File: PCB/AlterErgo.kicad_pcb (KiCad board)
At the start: 2 copper layers, 104 parts, among them J1 GS3, J2 SJ-43514, J3 GS3, J4 Conn_01x02, SW0:10 SW_Push, SW0:11 SW_Push, SW0:12 SW_Push, SW0:7 SW_Push, SW0:8 SW_Push, SW0:9 SW_Push, SW1 SW_SPST, SW1:10 SW_Push, SW1:11 SW_Push, SW1:12 SW_Push, SW1:13 SW_Push, SW1:7 SW_Push, SW1:8 SW_Push, SW1:9 SW_Push, SW2:10 SW_Push, SW2:11 SW_Push, SW2:12 SW_Push, SW2:13 SW_Push, SW2:7 SW_Push, SW2:8 SW_Push, SW2:9 SW_Push, SW3:10 SW_Push, SW3:11 SW_Push, SW3:12 SW_Push, SW3:13 SW_Push, SW3:8 SW_Push, SW3:9 SW_Push, SW4:10 SW_Push, SW4:11 SW_Push, SW4:12 SW_Push, SW4:13 SW_Push, SW4:7 SW_Push, SW4:8 SW_Push, SW4:9 SW_Push, SW5:10 SW_Push, SW5:11 SW_Push, SW5:12 SW_Push, SW5:13 SW_Push, SW5:7 SW_Push, SW5:8 SW_Push, SW5:9 SW_Push, U1 Feather32u4Bluefruit, U2 MCP23018

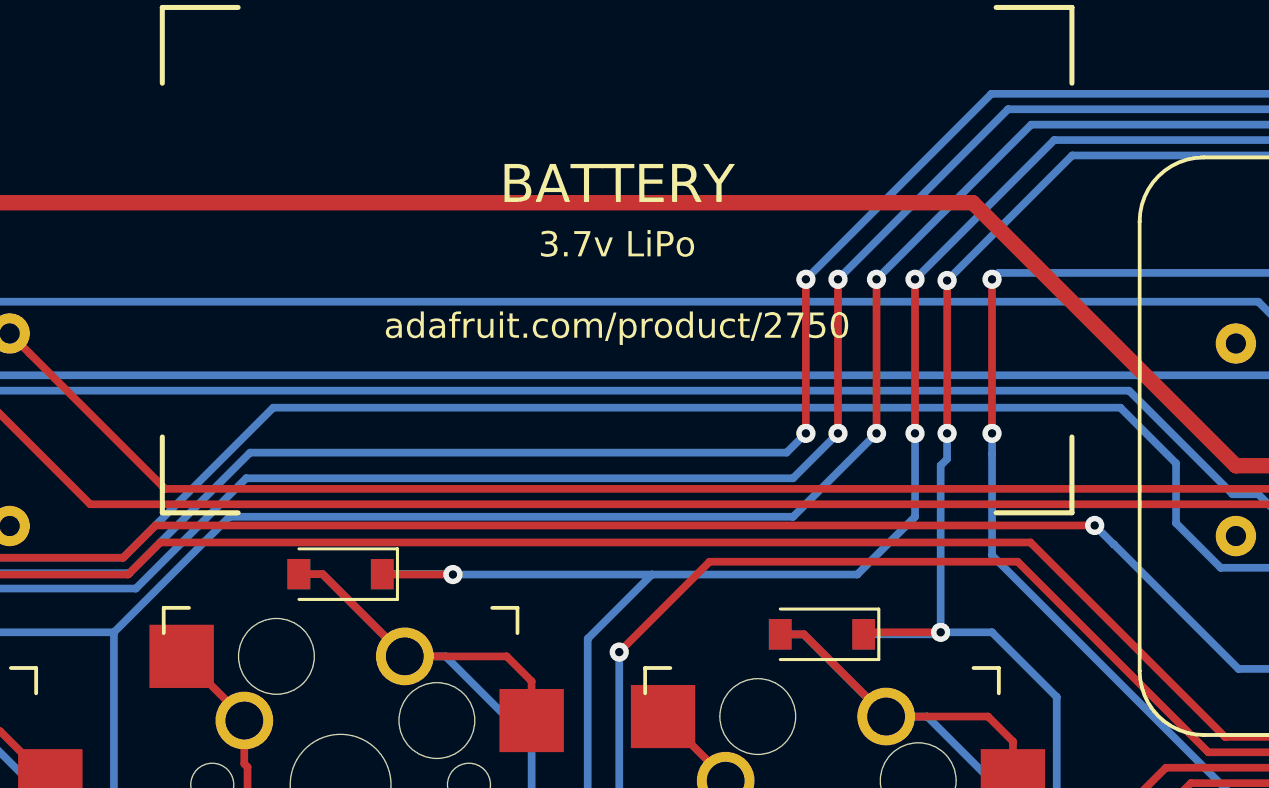
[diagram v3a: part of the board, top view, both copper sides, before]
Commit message: Correct some vias too close to other tracks
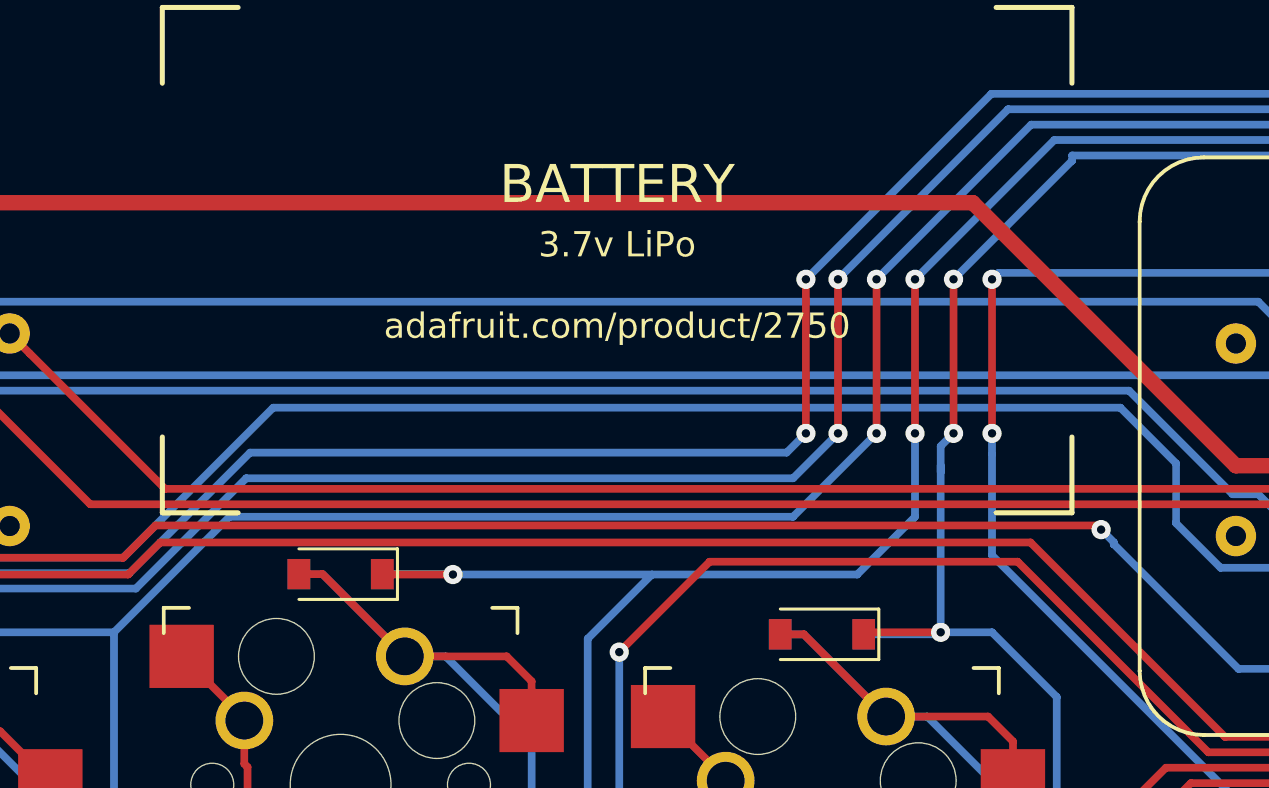
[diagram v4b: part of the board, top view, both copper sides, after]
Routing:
- net (no net): track 98.3 -> 29.2 mm
- net Net-(D1:13-Pad2): track 37.9 -> 59.3 mm
- net Net-(D4:13-Pad2): track 42.2 -> 60.0 mm
- net Net-(D3:13-Pad2): track 42.9 -> 60.4 mm
- net Net-(D2:13-Pad2): track 46.5 -> 58.8 mm
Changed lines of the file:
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@@
   (general
     (links 466)
-    (no_connects 453)
+    (no_connects 20)
     (area 33.589001 -2.08962 221.067701 182.523514)
     (thickness 1.6)
     (drawings 68)
-    (tracks 1728)
+    (tracks 1733)
     (zones 0)
     (modules 104)
@@
   (segment (start 192.7225 125.25375) (end 192.7225 118.070951) (width 0.3048) (layer F.Cu) (net 0))
   (segment (start 202.565 144.30375) (end 202.565 136.68375) (width 0.3048) (layer F.Cu) (net 0))
-  (segment (start 194.8815 133.477) (end 193.3575 131.953) (width 0.3048) (layer B.Cu) (net 0))
-  (segment (start 204.2795 133.477) (end 194.8815 133.477) (width 0.3048) (layer B.Cu) (net 0))
-  (segment (start 205.105 134.3025) (end 204.2795 133.477) (width 0.3048) (layer B.Cu) (net 0))
-  (segment (start 205.105 137.95375) (end 205.105 134.3025) (width 0.3048) (layer B.Cu) (net 0))
-  (segment (start 205.105 143.03375) (end 205.105 137.95375) (width 0.3048) (layer B.Cu) (net 0))
-  (segment (start 193.1035 113.157) (end 198.4375 113.157) (width 0.3048) (layer F.Cu) (net 0))
-  (segment (start 190.1825 116.078) (end 193.1035 113.157) (width 0.3048) (layer F.Cu) (net 0))
-  (segment (start 190.1825 118.90375) (end 190.1825 116.078) (width 0.3048) (layer F.Cu) (net 0))
-  (segment (start 192.3415 94.107) (end 198.1835 94.107) (width 0.3048) (layer B.Cu) (net 0))
-  (segment (start 190.1825 96.266) (end 192.3415 94.107) (width 0.3048) (layer B.Cu) (net 0))
-  (segment (start 190.1825 104.93375) (end 190.1825 96.266) (width 0.3048) (layer B.Cu) (net 0))
-  (segment (start 192.3415 75.057) (end 198.4375 75.057) (width 0.3048) (layer B.Cu) (net 0))
-  (segment (start 190.1825 77.216) (end 192.3415 75.057) (width 0.3048) (layer B.Cu) (net 0))
-  (segment (start 190.1825 85.88375) (end 190.1825 77.216) (width 0.3048) (layer B.Cu) (net 0))
   (segment (start 54.1655 128.905) (end 57.9755 128.905) (width 0.3048) (layer F.Cu) (net 1))
   (segment (start 57.9755 128.905) (end 68.1355 118.745) (width 0.3048) (layer F.Cu) (net 1))
@@
   (segment (start 108.7125 139.064808) (end 106.165876 139.064808) (width 0.3048) (layer F.Cu) (net 8))
   (segment (start 106.165876 139.064808) (end 105.523159 139.707525) (width 0.3048) (layer F.Cu) (net 8))
+  (segment (start 161.8615 39.751) (end 161.8615 40.005) (width 0.3048) (layer B.Cu) (net 9))
+  (segment (start 161.8615 40.005) (end 161.8615 46.355) (width 0.3048) (layer B.Cu) (net 9))
+  (segment (start 162.3695 38.481) (end 161.8615 38.989) (width 0.3048) (layer B.Cu) (net 9))
+  (segment (start 161.8615 38.989) (end 161.8615 40.005) (width 0.3048) (layer B.Cu) (net 9))
+  (segment (start 162.3695 38.227) (end 162.3695 38.481) (width 0.3048) (layer F.Cu) (net 9))
+  (via (at 162.3695 38.481) (size 0.762) (drill 0.3302) (layers F.Cu B.Cu) (net 9))
+  (segment (start 162.3695 32.385) (end 162.3695 38.227) (width 0.3048) (layer F.Cu) (net 9))
+  (segment (start 167.065425 27.482799) (end 167.065425 27.689075) (width 0.3048) (layer B.Cu) (net 9))
+  (segment (start 167.065425 27.689075) (end 162.3695 32.385) (width 0.3048) (layer B.Cu) (net 9))
+  (via (at 162.3695 32.385) (size 0.762) (drill 0.3302) (layers F.Cu B.Cu) (net 9))
   (segment (start 166.454701 48.916201) (end 166.454701 60.557799) (width 0.3048) (layer B.Cu) (net 9))
   (segment (start 93.69375 151.447692) (end 93.69375 152.43125) (width 0.3048) (layer B.Cu) (net 9))
@@
   (segment (start 161.988499 65.024001) (end 161.6075 65.405) (width 0.3048) (layer B.Cu) (net 9))
   (segment (start 161.8615 46.355) (end 163.8935 46.355) (width 0.3048) (layer B.Cu) (net 9))
-  (segment (start 162.1155 39.497) (end 161.8615 39.751) (width 0.3048) (layer B.Cu) (net 9))
-  (segment (start 161.8615 39.751) (end 161.8615 46.355) (width 0.3048) (layer B.Cu) (net 9))
   (segment (start 161.6075 122.555) (end 158.891875 122.555) (width 0.3048) (layer F.Cu) (net 9))
   (segment (start 158.891875 122.555) (end 158.8125 122.634375) (width 0.3048) (layer F.Cu) (net 9))
@@
   (segment (start 161.782125 46.434375) (end 161.8615 46.355) (width 0.3048) (layer B.Cu) (net 9))
   (via (at 161.8615 46.355) (size 0.762) (drill 0.3302) (layers F.Cu B.Cu) (net 9))
-  (segment (start 162.1155 38.481) (end 162.1155 39.497) (width 0.3048) (layer B.Cu) (net 9))
-  (segment (start 162.1155 32.432724) (end 162.1155 38.481) (width 0.3048) (layer F.Cu) (net 9))
-  (via (at 162.1155 38.481) (size 0.762) (drill 0.3302) (layers F.Cu B.Cu) (net 9))
   (segment (start 193.8655 28.829) (end 192.519299 27.482799) (width 0.3048) (layer B.Cu) (net 9))
   (segment (start 192.519299 27.482799) (end 167.065425 27.482799) (width 0.3048) (layer B.Cu) (net 9))
-  (segment (start 167.065425 27.482799) (end 162.1155 32.432724) (width 0.3048) (layer B.Cu) (net 9))
-  (via (at 162.1155 32.432724) (size 0.762) (drill 0.3302) (layers F.Cu B.Cu) (net 9))
   (segment (start 191.3255 34.925) (end 193.8655 32.385) (width 0.3048) (layer F.Cu) (net 9))
   (segment (start 193.8655 32.385) (end 193.8655 28.829) (width 0.3048) (layer F.Cu) (net 9))
@@
   (segment (start 186.2455 34.925) (end 182.9435 31.623) (width 0.3048) (layer F.Cu) (net 21))
   (segment (start 179.514499 29.717999) (end 178.6255 28.829) (width 0.3048) (layer F.Cu) (net 21))
+  (segment (start 194.8815 133.477) (end 193.3575 131.953) (width 0.3048) (layer B.Cu) (net 22))
+  (segment (start 204.2795 133.477) (end 194.8815 133.477) (width 0.3048) (layer B.Cu) (net 22))
+  (segment (start 205.105 134.3025) (end 204.2795 133.477) (width 0.3048) (layer B.Cu) (net 22))
+  (segment (start 205.105 137.95375) (end 205.105 134.3025) (width 0.3048) (layer B.Cu) (net 22))
+  (segment (start 205.105 143.03375) (end 205.105 137.95375) (width 0.3048) (layer B.Cu) (net 22))
   (segment (start 193.6125 132.206) (end 187.7025 138.116) (width 0.3048) (layer F.Cu) (net 22))
   (segment (start 187.7025 138.116) (end 187.7025 143.03375) (width 0.3048) (layer F.Cu) (net 22))
@@
   (segment (start 174.5625 113.109375) (end 175.498125 113.109375) (width 0.3048) (layer F.Cu) (net 29))
   (segment (start 175.498125 113.109375) (end 178.7525 116.36375) (width 0.3048) (layer F.Cu) (net 29))
+  (segment (start 193.1035 113.157) (end 198.4375 113.157) (width 0.3048) (layer F.Cu) (net 30))
+  (segment (start 190.1825 116.078) (end 193.1035 113.157) (width 0.3048) (layer F.Cu) (net 30))
+  (segment (start 190.1825 118.90375) (end 190.1825 116.078) (width 0.3048) (layer F.Cu) (net 30))
   (segment (start 206.0575 115.697) (end 207.585 117.2245) (width 0.3048) (layer B.Cu) (net 30))
   (segment (start 207.585 117.2245) (end 207.585 123.98375) (width 0.3048) (layer B.Cu) (net 30))
@@
   (segment (start 174.5625 94.059375) (end 175.498125 94.059375) (width 0.3048) (layer F.Cu) (net 36))
   (segment (start 175.498125 94.059375) (end 178.7525 97.31375) (width 0.3048) (layer F.Cu) (net 36))
+  (segment (start 192.3415 94.107) (end 198.1835 94.107) (width 0.3048) (layer B.Cu) (net 37))
+  (segment (start 190.1825 96.266) (end 192.3415 94.107) (width 0.3048) (layer B.Cu) (net 37))
+  (segment (start 190.1825 104.93375) (end 190.1825 96.266) (width 0.3048) (layer B.Cu) (net 37))
   (segment (start 200.9775 96.901) (end 204.63225 96.901) (width 0.3048) (layer F.Cu) (net 37))
   (segment (start 204.63225 96.901) (end 207.585 99.85375) (width 0.3048) (layer F.Cu) (net 37))
@@
   (segment (start 174.5625 75.009375) (end 175.498125 75.009375) (width 0.3048) (layer F.Cu) (net 43))
   (segment (start 175.498125 75.009375) (end 178.7525 78.26375) (width 0.3048) (layer F.Cu) (net 43))
+  (segment (start 192.3415 75.057) (end 198.4375 75.057) (width 0.3048) (layer B.Cu) (net 44))
+  (segment (start 190.1825 77.216) (end 192.3415 75.057) (width 0.3048) (layer B.Cu) (net 44))
+  (segment (start 190.1825 85.88375) (end 190.1825 77.216) (width 0.3048) (layer B.Cu) (net 44))
   (segment (start 206.5655 78.359) (end 207.585 79.3785) (width 0.3048) (layer B.Cu) (net 44))
   (segment (start 207.585 79.3785) (end 207.585 85.88375) (width 0.3048) (layer B.Cu) (net 44))
@@
   (segment (start 186.512299 43.802201) (end 182.054499 48.260001) (width 0.3048) (layer F.Cu) (net 60))
   (segment (start 182.054499 48.260001) (end 181.1655 49.149) (width 0.3048) (layer F.Cu) (net 60))
-  (segment (start 167.9575 42.125999) (end 130.784501 42.125999) (width 0.3048) (layer F.Cu) (net 61))
+  (segment (start 168.2115 42.291) (end 168.7195 42.799) (width 0.3048) (layer B.Cu) (net 61))
+  (segment (start 168.7195 42.799) (end 168.7195 42.8752) (width 0.3048) (layer B.Cu) (net 61))
+  (segment (start 130.784501 42.125999) (end 168.046499 42.125999) (width 0.3048) (layer F.Cu) (net 61))
+  (segment (start 168.046499 42.125999) (end 168.2115 42.291) (width 0.3048) (layer F.Cu) (net 61))
+  (via (at 168.2115 42.291) (size 0.762) (drill 0.3302) (layers F.Cu B.Cu) (net 61))
   (segment (start 130.784501 42.125999) (end 129.505174 43.405326) (width 0.3048) (layer F.Cu) (net 61))
   (segment (start 129.505174 43.405326) (end 109.381826 43.405326) (width 0.3048) (layer F.Cu) (net 61))
@@
   (segment (start 105.814 39.8375) (end 83.6125 39.8375) (width 0.3048) (layer F.Cu) (net 61))
   (segment (start 168.7195 42.8752) (end 168.706701 42.8752) (width 0.3048) (layer B.Cu) (net 61))
-  (via (at 167.9575 42.125999) (size 0.762) (drill 0.3302) (layers F.Cu B.Cu) (net 61))
-  (segment (start 168.706701 42.8752) (end 167.9575 42.125999) (width 0.3048) (layer B.Cu) (net 61))
   (segment (start 168.7195 42.8752) (end 173.647099 47.802799) (width 0.3048) (layer B.Cu) (net 61))
   (segment (start 173.647099 47.802799) (end 200.139299 47.802799) (width 0.3048) (layer B.Cu) (net 61))

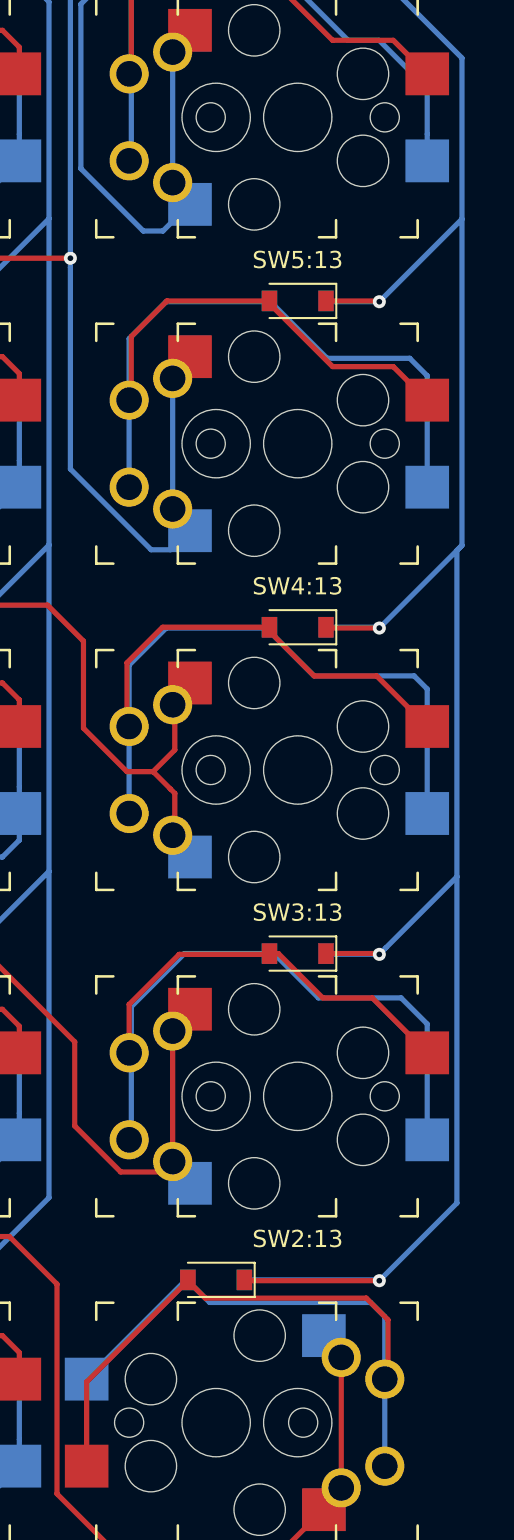
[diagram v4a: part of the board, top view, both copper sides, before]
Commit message: Adjust outer column socket footprint to avoid overlapping drill holes
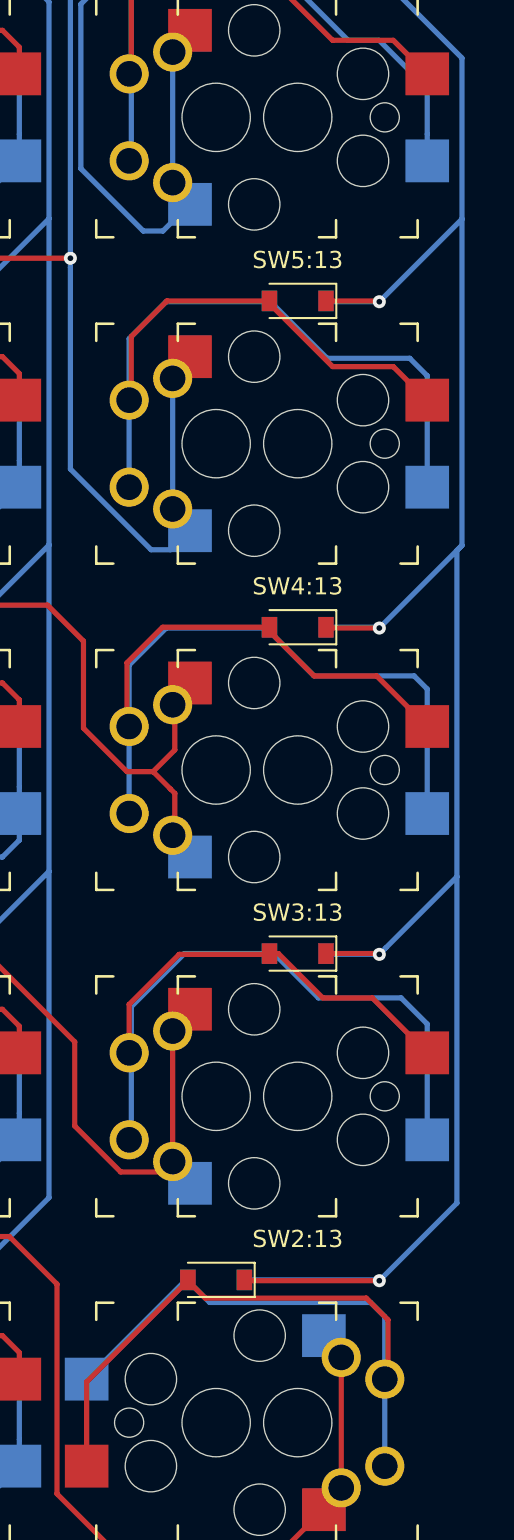
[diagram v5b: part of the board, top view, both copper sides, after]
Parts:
- SW1:13, SW2:13, SW3:13, SW4:13, SW5:13: footprint keyswitches:Kailh_socket_reversible -> AlterErgo:Kailh_socket_reversible_nohole
